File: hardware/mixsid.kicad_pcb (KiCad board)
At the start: 2 copper layers, 61 x 55.9 mm, 69 parts, among them P1 INPUT, P2 CONTROL, P4 SOCKET LEFT, P5 OUTPUT, P6 SOCKET RIGHT, Q1 BC547, Q2 BC547, U1 GAL16V8, U2 SID2, U3 7812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

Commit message: Hardware: Rerouting in progress...
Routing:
- net /+12V: track 142.7 -> 154.2 mm
- net /+9V: track 77.3 -> 85.0 mm
- net /M0: track 69.2 -> 73.3 mm
- net /~IO2EN: track 75.2 -> 79.0 mm
- net Net-(C21-Pad2): track 13.8 -> 17.5 mm
- net /~CS1: track 9.19 -> 12.5 mm
- net /D3: track 23.3 -> 26.4 mm
- net VCC: track 75.9 -> 78.9 mm
- net /S2IN: track 17.8 -> 20.8 mm
- net /POTY1: track 11.4 -> 14.3 mm
- net Net-(C11-Pad1): track 12.4 -> 14.8 mm
- net /~IO1EN: track 58.2 -> 59.9 mm
- net Net-(JP6-Pad2): track 20.5 -> 22.1 mm
- net /MS: track 55.6 -> 57.0 mm
- net Net-(C19-Pad2): track 16.2 -> 17.5 mm
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
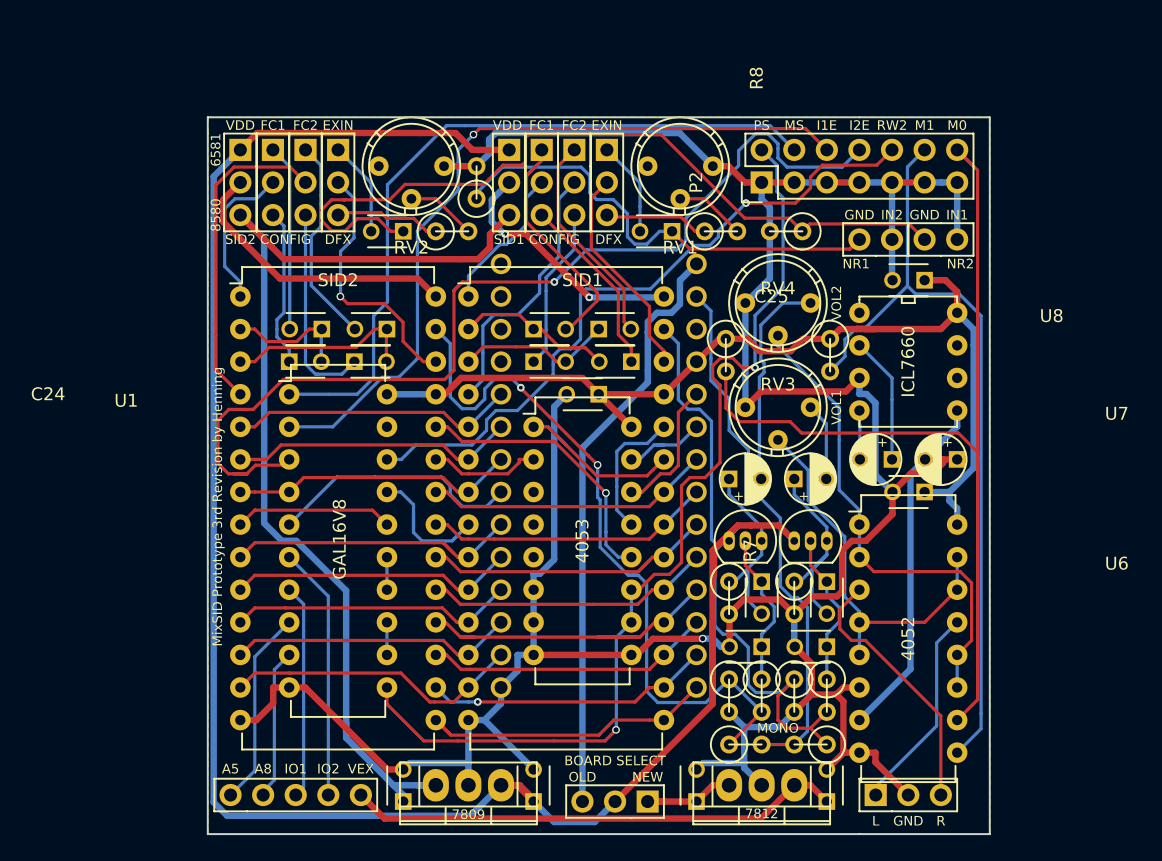
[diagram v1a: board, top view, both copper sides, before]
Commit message: Hardware: Improved routing, silkscreen
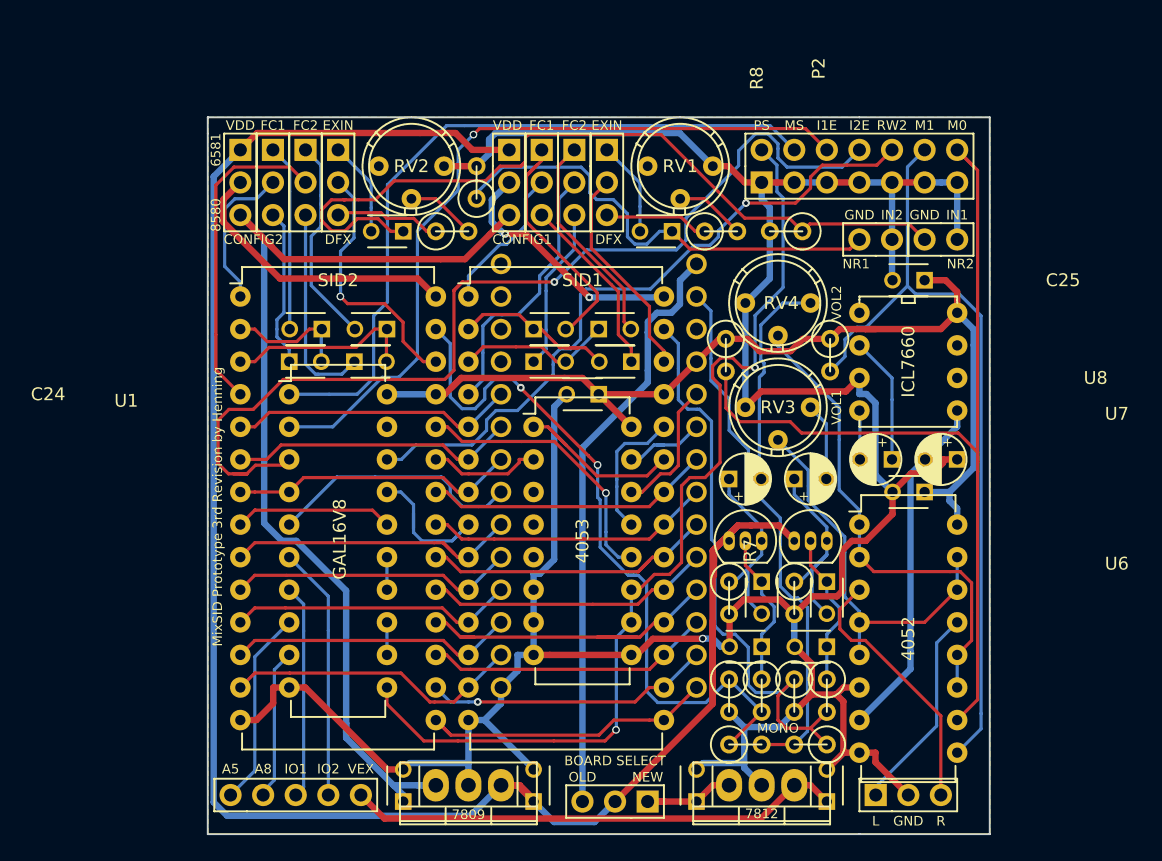
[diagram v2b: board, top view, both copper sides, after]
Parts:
- P2: footprint Pin_Headers:Pin_Header_Straight_2x07 -> Pinheaders:Pin_Header_Straight_2x07
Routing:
- net /+9V: track 85.0 -> 84.4 mm
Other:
- board text added: "CONFIG1"
- board text added: "CONFIG2"
- board text removed: "SID1 CONFIG"
- board text removed: "SID2 CONFIG"

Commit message: Hardware: Use rect pots for digifix again, placed volume pods horizontally
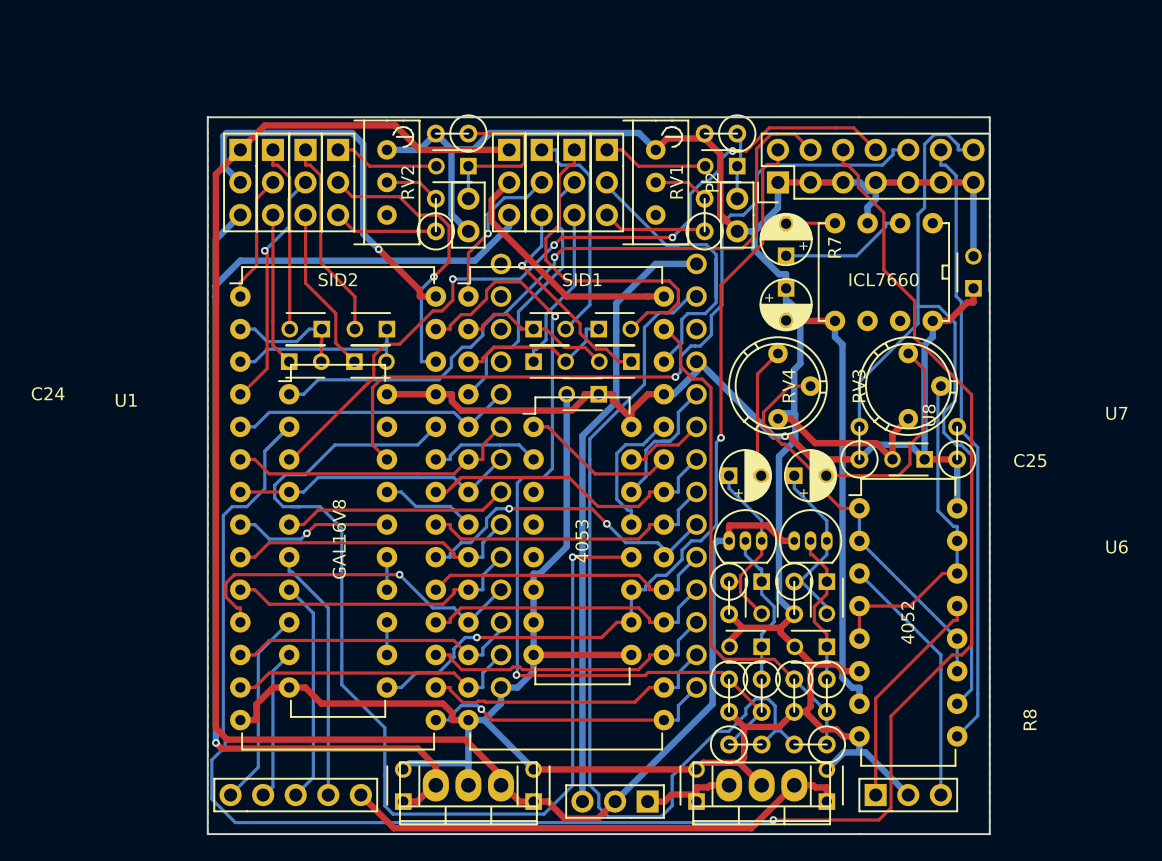
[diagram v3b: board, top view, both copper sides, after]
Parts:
- P2: footprint Pinheaders:Pin_Header_Straight_2x07 -> Pin_Headers:Pin_Header_Straight_2x07
- RV1, RV2: footprint Potentiometers:Potentiometer_Bourns_3339P_Angular_ScrewUp -> Potentiometers:Potentiometer_Bourns_3296W_3-8Zoll_Inline_ScrewUp
- moved JP10 35.7 mm to (148.6, 73.7), turned to 0 degrees
- moved R9 27.1 mm to (147.3, 68.6)
- moved R2 19.4 mm to (168.3, 68.6), turned to 180 degrees
- moved C18 18.9 mm to (173.4, 80.6), turned to 270 degrees
- moved C17 17.9 mm to (173.4, 78.1), turned to 90 degrees
- moved C23 16.3 mm to (188.0, 80.6), turned to 90 degrees
- moved C25 14.0 mm to (184.2, 94.0)
- moved R7 12.5 mm to (179.1, 92.7), turned to 90 degrees
- moved R8 12.0 mm to (186.7, 92.7), turned to 90 degrees
- moved JP9 10.0 mm to (169.5, 73.7), turned to 0 degrees
- moved U8 9.03 mm to (184.8, 75.6), turned to 270 degrees
- moved RV4 8.70 mm to (182.9, 85.7), turned to 270 degrees
- moved C13 7.18 mm to (148.6, 71.1)
- moved C14 7.18 mm to (169.5, 71.1)
- moved RV3 4.69 mm to (172.7, 85.7), turned to 270 degrees
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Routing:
- net /~IO1EN: track 59.9 -> 147.9 mm
- net /POTX2: track 21.8 -> 83.5 mm
- net Net-(C13-Pad1): track 63.2 -> 13.5 mm
- net Net-(C14-Pad1): track 37.3 -> 5.30 mm
- net /MONO_OUT: track 42.1 -> 69.6 mm
- net /~IO2EN: track 79.0 -> 60.7 mm, vias 1 -> 4
- net /+12V: track 154.2 -> 136.1 mm
- net GND: track 244.0 -> 259.3 mm, vias 1 -> 0
- net /M1: track 62.3 -> 48.1 mm
- net /PS: track 76.9 -> 65.2 mm
- net Net-(C22-Pad2): track 6.10 -> 16.5 mm
- net Net-(C9-Pad2): track 16.8 -> 26.6 mm
- net /S2OUT: track 57.2 -> 66.7 mm
- net /M0: track 73.3 -> 64.0 mm
- net /~RW2: track 53.5 -> 62.2 mm
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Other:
- board text removed: "6581"
- board text removed: "7809"
- board text removed: "7812"
- board text removed: "8580"
- board text removed: "A5"
- board text removed: "A8"
- board text removed: "BOARD SELECT"
- board text removed: "CONFIG1"
- board text removed: "CONFIG2"
- board text removed: "DFX"
- board text removed: "EXIN"
- board text removed: "FC1"
- board text removed: "FC2"
- board text removed: "GND"
- board text removed: "I1E"
- board text removed: "I2E"
- board text removed: "IN1"
- board text removed: "IN2"
- board text removed: "IO1"
- board text removed: "IO2"
- board text removed: "L"
- board text removed: "M0"
- board text removed: "M1"
- board text removed: "MONO"
- board text removed: "MS"
- board text removed: "MixSID Prototype 3rd Revision by Henning"
- board text removed: "NEW"
- board text removed: "NR1"
- board text removed: "NR2"
- board text removed: "OLD"
- board text removed: "PS"
- board text removed: "R"
- board text removed: "RW2"
- board text removed: "VDD"
- board text removed: "VEX"
- board text removed: "VOL1"
- board text removed: "VOL2"

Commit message: Hardware: Improved routing, silkscreen and rendering
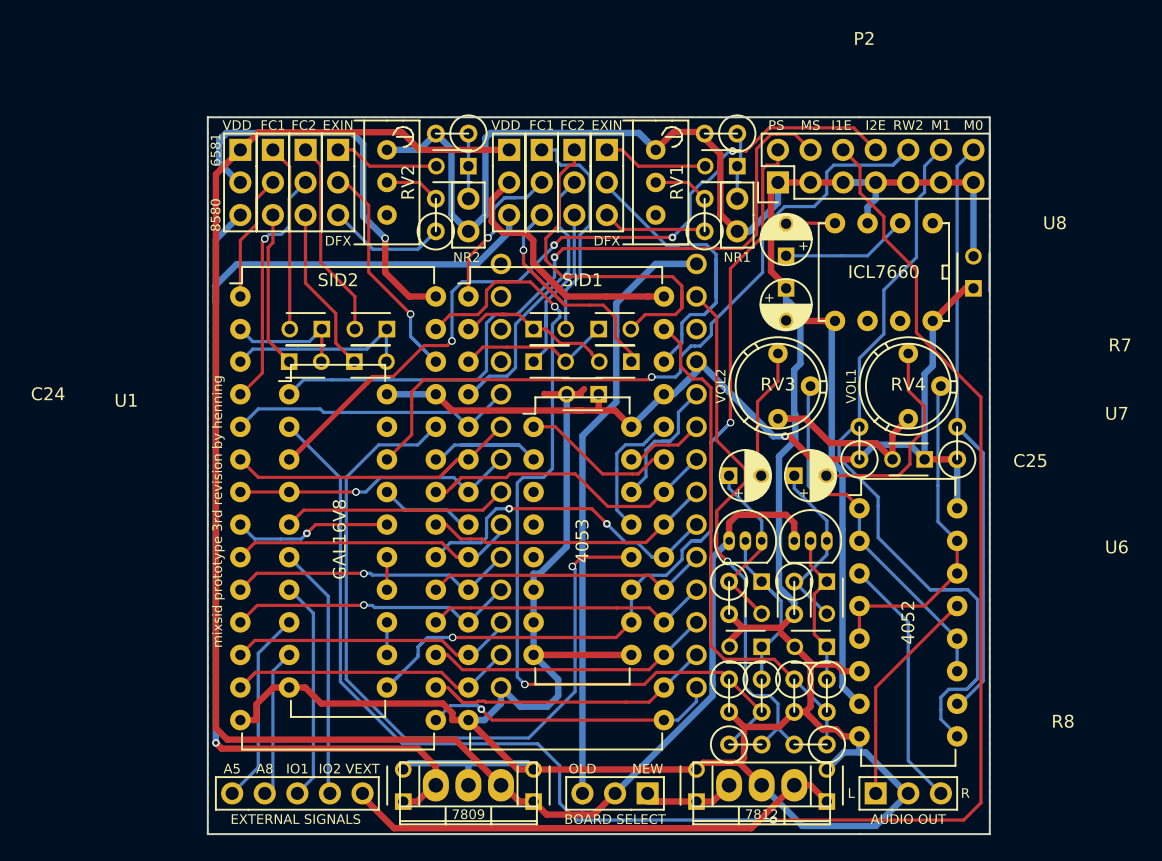
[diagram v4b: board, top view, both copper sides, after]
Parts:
- moved R7 7.62 mm to (186.7, 92.7)
- moved R8 7.62 mm to (179.1, 92.7)
- moved JP4 0.64 mm to (162.6, 120.0)
- moved P1 0.18 mm to (130.2, 120.0)
- moved P5 0.13 mm to (180.3, 120.0)
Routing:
- net GND: track 259.3 -> 295.3 mm
- net /MONO_OUT: track 69.6 -> 42.8 mm, vias 0 -> 1
- net /POTX2: track 83.5 -> 60.8 mm
- net /M0: track 64.0 -> 48.2 mm
- net /~IO1EN: track 147.9 -> 133.5 mm
- net /M1: track 48.1 -> 61.3 mm
- net Net-(C12-Pad1): track 16.6 -> 28.8 mm
- net /~IO2EN: track 60.7 -> 70.2 mm
- net Net-(C13-Pad1): track 13.5 -> 5.08 mm
- net /A2: track 28.0 -> 22.6 mm
- net Net-(JP6-Pad2): track 21.0 -> 26.0 mm
- net /PS: track 65.2 -> 70.0 mm
- net /POTY2: track 8.72 -> 13.1 mm
- net /PWR1: track 19.5 -> 23.8 mm
- net /MS: track 54.6 -> 58.7 mm
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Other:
- board text added: "6581"
- board text added: "7809"
- board text added: "7812"
- board text added: "8580"
- board text added: "A5"
- board text added: "A8"
- board text added: "AUDIO OUT"
- board text added: "BOARD SELECT"
- board text added: "DFX"
- board text added: "EXIN"
- board text added: "EXTERNAL SIGNALS"
- board text added: "FC1"
- board text added: "FC2"
- board text added: "I1E"
- board text added: "I2E"
- board text added: "IO1"
- board text added: "IO2"
- board text added: "L"
- board text added: "M0"
- board text added: "M1"
- board text added: "MS"
- board text added: "NEW"
- board text added: "NR1"
- board text added: "NR2"
- board text added: "OLD"
- board text added: "PS"
- board text added: "R"
- board text added: "RW2"
- board text added: "VDD"
- board text added: "VEXT"
- board text added: "VOL1"
- board text added: "VOL2"
- board text added: "mixsid prototype 3rd revision by henning"

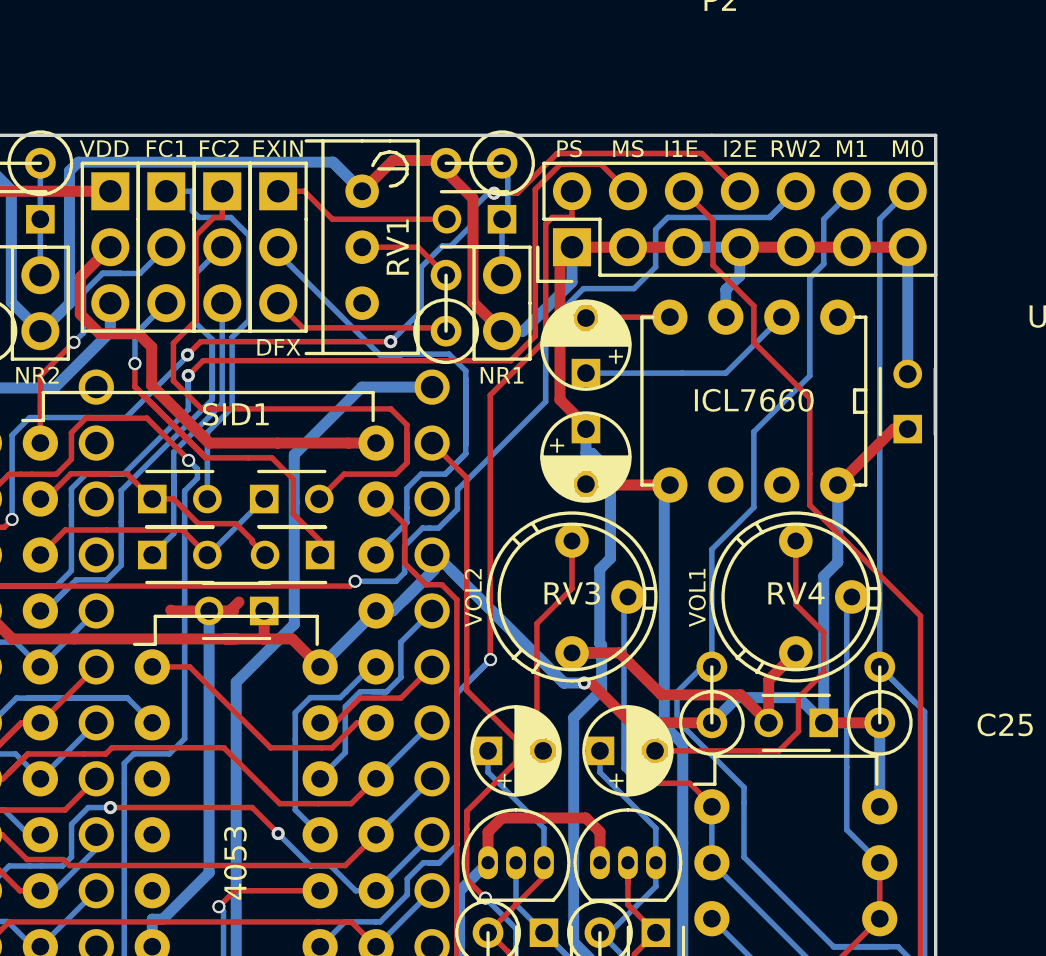
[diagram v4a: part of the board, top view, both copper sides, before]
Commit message: Hardware: Swapped MS/PS, improved routing, silkscreen
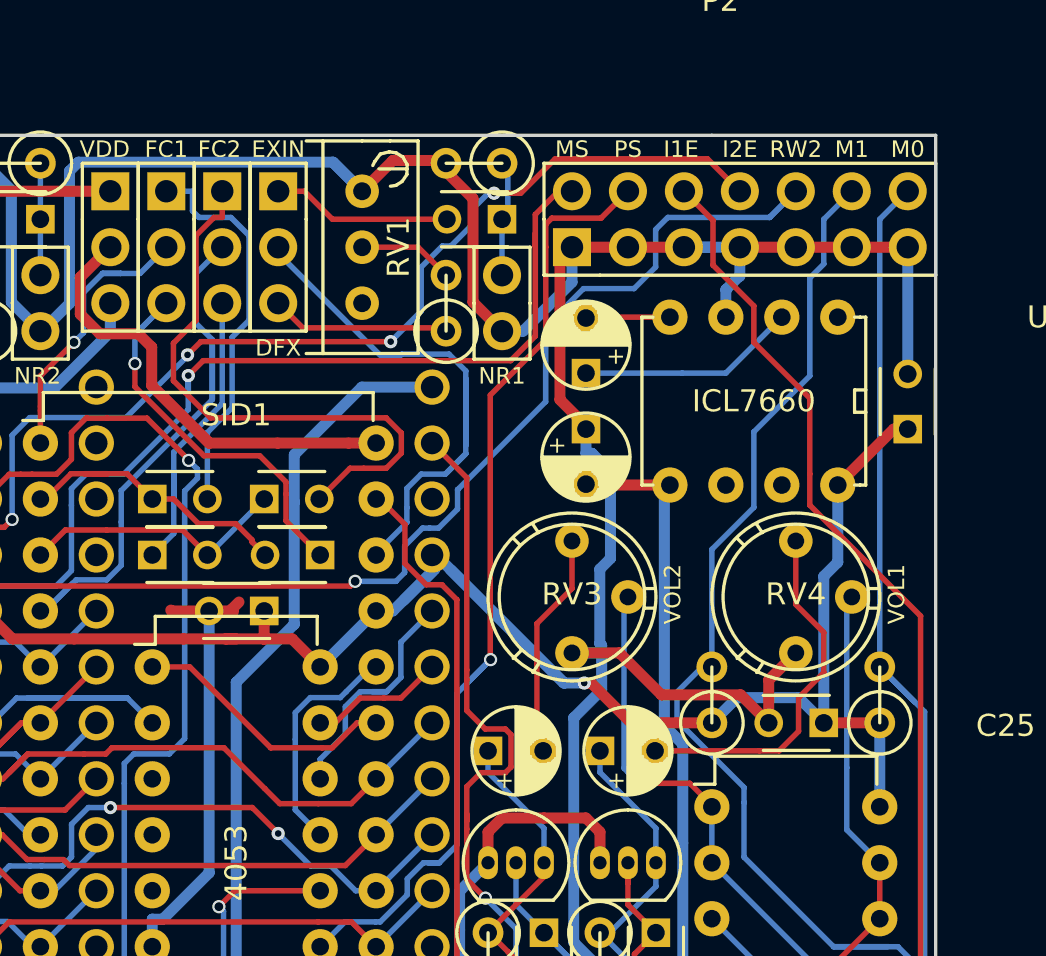
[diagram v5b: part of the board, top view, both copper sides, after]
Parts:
- P2: footprint Pin_Headers:Pin_Header_Straight_2x07 -> Pinheaders:Pin_Header_Straight_2x07
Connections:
- P2 pad 2: /PS -> /MS
- P2 pad 4: /MS -> /PS
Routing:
- net Net-(C12-Pad1): track 28.8 -> 19.4 mm
- net /MS: track 58.7 -> 55.1 mm
- net Net-(C9-Pad2): track 28.8 -> 26.6 mm
- net /PS: track 70.0 -> 71.8 mm
- net /MONO_OUT: track 42.8 -> 43.8 mm

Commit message: Hardware: Prototype 3: Added gerber files for production
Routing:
- net VCC: track 83.1 -> 72.9 mm
- net Net-(C11-Pad2): track 17.9 -> 17.3 mm

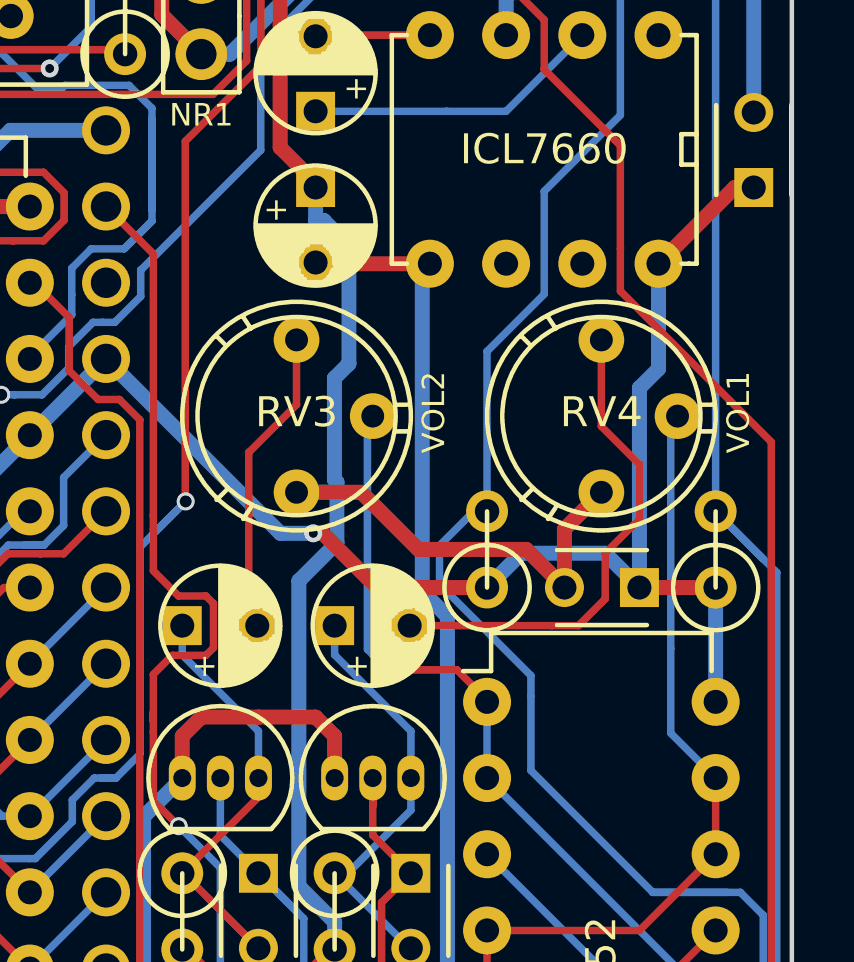
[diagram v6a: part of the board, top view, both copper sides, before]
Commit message: Hardware: Fixed connection and orientation of volume pots
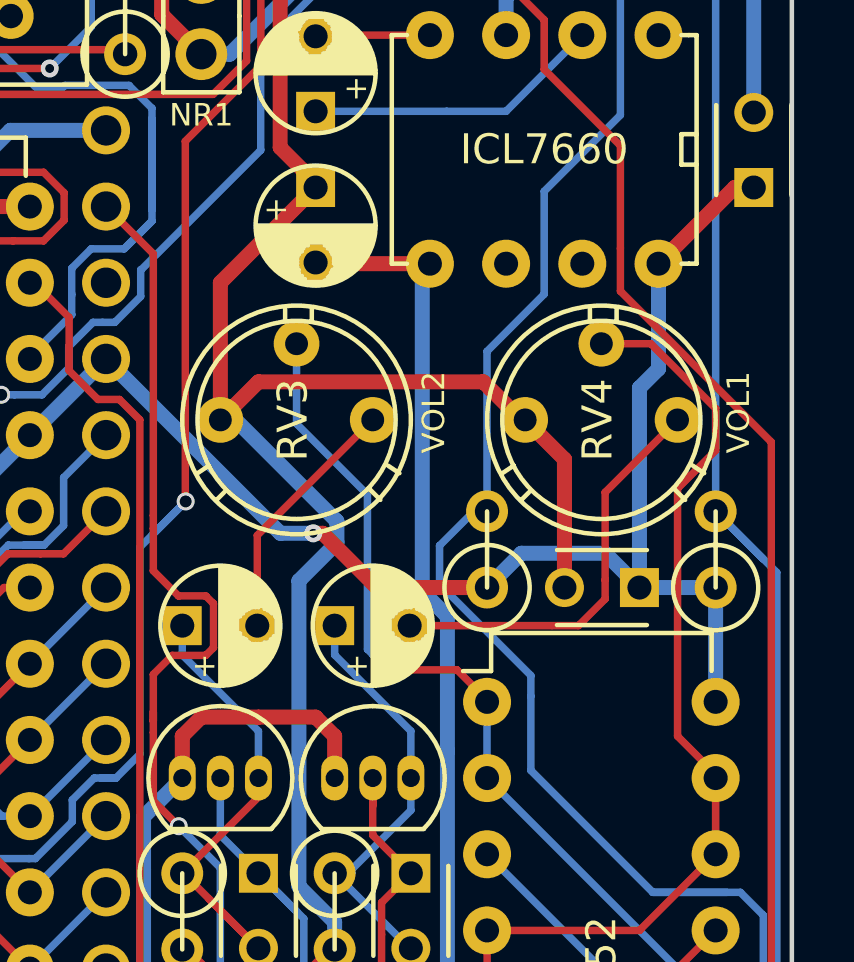
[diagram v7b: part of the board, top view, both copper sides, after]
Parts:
- moved RV3 3.68 mm to (170.2, 88.4), turned to 0 degrees
- moved RV4 3.68 mm to (180.3, 88.4), turned to 0 degrees
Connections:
- RV3 pad 1: Net-(C19-Pad2) -> GND
- RV3 pad 3: GND -> Net-(C19-Pad2)
- RV4 pad 1: Net-(C22-Pad2) -> GND
- RV4 pad 3: GND -> Net-(C22-Pad2)
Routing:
- net /RIGHT: track 26.5 -> 31.8 mm
- net GND: track 295.3 -> 299.8 mm
- net /LEFT: track 29.2 -> 32.5 mm
- net Net-(C22-Pad2): track 16.5 -> 14.2 mm
- net Net-(C19-Pad2): track 10.3 -> 8.45 mm
